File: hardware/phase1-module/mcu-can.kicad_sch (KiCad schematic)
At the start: 29 parts, among them J2 SWD, J3 UART, U10 STM32G431CBT6, U11 TCAN1042HGV, Y1 8MHz

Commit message: Apply China-sourcing engineering changes across all boards + mechanical frame
All datasheet-verified before application (details hardware/SOURCING.md sF):
- TMUX1101 -> TS5A3166DBVR (LCSC availability; ts5a3166.pdf: pin POSITIONS
  identical - 1=NO 2=COM 3=GND 4=IN 5=V+; VIH 2.4V ok from 3.3V GPIO)
- TLV7011 DBVR -> DCKR: tlv7022.pdf shows DBV/DCK share one pinout, so
  footprint-only (SOT-353_SC-70-5); SOT-23-5 stock in China is nearly gone
- crystal load caps 10p -> 18p, both phases (CL=12pF China crystals; the
  HANDOVER-blessed alternative to hunting CL=8pF parts)
- Phase-1 inductor -> MWSA1707S-100MT (JLCPCB-verified 16.5A Isat/10.5A
  Irms vs 12A/8A required); value strings now dual-source Sunlord/Coilcraft
- module slot power + P2 output -> XT60PW-M (2-pin), backplane slots ->
  XT60PW-F; bus shunt -> 2x BVS-M-R0005 parallel (the exact-net checker
  caught RS1/RS2 placed one pin-span apart merging VBUS_IN into VBUS)
- 470u bulk -> THT radial D10; output MLCCs 22u -> 10u/50V X7S; buzzer ->
  MLT-8530 (fp placeholder)
All four checker chains green: 137/173/30/80 components.

hardware/MECHANICAL.md (frozen): 30mm slot pitch, P2 130x90 4-layer,
backplane ~330x100 2-layer 2oz, manager 100x80; cost-first stackup (1oz
outer + solder-reinforced bus, 2oz only if the thermal soak demands it);
inductor footprint = SUPERSET pattern accepting Sunlord 1707 AND Coilcraft
XAL1510 so the A/B pair is a pure part swap.

HANDOVER: sub-0.5V mV-accurate output DEFERRED to a future dedicated
linear post-regulator module (user decision 2026-07-18); buck floors
documented (P2 0.7V @30V bus, P1 0.5V).

Co-Authored-By: Claude Fable 5 <noreply@anthropic.com>
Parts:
- C66, C67: value 10p -> 18p
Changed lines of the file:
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@@
     (in_bom yes) (on_board yes) (dnp no)
     (property "Reference" "C66" (at 213.35999999999999 132.07999999999998 0) (effects (font (size 1.27 1.27)) (justify left)))
-    (property "Value" "10p" (at 213.35999999999999 134.62 0) (effects (font (size 1.27 1.27)) (justify left)))
+    (property "Value" "18p" (at 213.35999999999999 134.62 0) (effects (font (size 1.27 1.27)) (justify left)))
     (property "Footprint" "Capacitor_SMD:C_0603_1608Metric" (at 210.82 137.16 0) (effects (font (size 1.27 1.27)) hide))
     (property "Datasheet" "~" (at 210.82 137.16 0) (effects (font (size 1.27 1.27)) hide))
@@
     (in_bom yes) (on_board yes) (dnp no)
     (property "Reference" "C67" (at 228.6 132.07999999999998 0) (effects (font (size 1.27 1.27)) (justify left)))
-    (property "Value" "10p" (at 228.6 134.62 0) (effects (font (size 1.27 1.27)) (justify left)))
+    (property "Value" "18p" (at 228.6 134.62 0) (effects (font (size 1.27 1.27)) (justify left)))
     (property "Footprint" "Capacitor_SMD:C_0603_1608Metric" (at 226.06 137.16 0) (effects (font (size 1.27 1.27)) hide))
     (property "Datasheet" "~" (at 226.06 137.16 0) (effects (font (size 1.27 1.27)) hide))

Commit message: Add LCSC part numbers to all four boards' schematics and generate BOMs
common/bom.py writes hidden LCSC/MPN/Manufacturer properties into the
placed symbols (additive only, both one-line and KiCad multi-line
property styles) and emits <board>/bom/<board>-bom.csv plus a
JLCPCB-format CSV. Part table in common/lcsc_parts.py, transcribed
from SOURCING.md with explicit references per board; CHECK notes flag
footprint/variant mismatches. --check fails on stale output.

Co-Authored-By: Claude Opus 5.5 (1M context) <noreply@anthropic.com>
Claude-Session: https://claude.ai/code/session_01MKtKgebN9BpUrgqHq9t7pT
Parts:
- U10: LCSC (none) -> C529355; MPN (none) -> STM32G431CBT6; Manufacturer (none) -> ST
- U11: LCSC (none) -> C485806; MPN (none) -> TCAN1042VDRQ1; Manufacturer (none) -> TI
- Y1: LCSC (none) -> C400090
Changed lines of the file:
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@@
     (property "Footprint" "Package_QFP:LQFP-48_7x7mm_P0.5mm" (at 88.9 116.84 0) (effects (font (size 1.27 1.27)) hide))
     (property "Datasheet" "~" (at 88.9 116.84 0) (effects (font (size 1.27 1.27)) hide))
+    (property "LCSC" "C529355" (at 88.9 116.84 0) (effects (font (size 1.27 1.27)) hide))
+    (property "MPN" "STM32G431CBT6" (at 88.9 116.84 0) (effects (font (size 1.27 1.27)) hide))
+    (property "Manufacturer" "ST" (at 88.9 116.84 0) (effects (font (size 1.27 1.27)) hide))
     (pin "1")
     (pin "10")
@@
     (property "Footprint" "Crystal:Crystal_SMD_3225-4Pin_3.2x2.5mm" (at 218.44 127.0 0) (effects (font (size 1.27 1.27)) hide))
     (property "Datasheet" "~" (at 218.44 127.0 0) (effects (font (size 1.27 1.27)) hide))
+    (property "LCSC" "C400090" (at 218.44 127.0 0) (effects (font (size 1.27 1.27)) hide))
     (pin "1")
     (pin "2")
@@
     (property "Footprint" "Package_SO:SOIC-8_3.9x4.9mm_P1.27mm" (at 174.5 165.1 0) (effects (font (size 1.27 1.27)) hide))
     (property "Datasheet" "~" (at 174.5 165.1 0) (effects (font (size 1.27 1.27)) hide))
-    (pin "1")
-    (pin "2")
+    (property "LCSC" "C485806" (at 174.5 165.1 0) (effects (font (size 1.27 1.27)) hide))
+    (property "MPN" "TCAN1042VDRQ1" (at 174.5 165.1 0) (effects (font (size 1.27 1.27)) hide))
+    (property "Manufacturer" "TI" (at 174.5 165.1 0) (effects (font (size 1.27 1.27)) hide))
+    (pin "1")
+    (pin "2")

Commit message: Phase-1 BOM: LCSC numbers for every assembled part
Fill the 109 missing Phase-1 placements from the JLCPCB catalogue
(checked 2026-09-27, Basic parts where one fits), so 127 of 136
placements carry an LCSC number. J1-J6 and F1 stay hand-solder;
C17 and R17 are DNP.

Out-of-stock swaps: Q1-Q4 CSD18563Q5A -> NTMFS5C670NLT1G (SO-8FL,
same pinout), P1 U5 INA228AIDGSR -> INA228AQDGSRQ1. Y1 moves to the
CL = 12 pF version of the same crystal (C400090 was the 10 pF one).

Co-Authored-By: Claude Opus 5.5 (1M context) <noreply@anthropic.com>
Claude-Session: https://claude.ai/code/session_013uVohQZFdivAh43gw4mZtf
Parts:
- C62, C68, C69, C70, C71, C72, C73, C74: LCSC (none) -> C14663; MPN (none) -> CC0603KRX7R9BB104; Manufacturer (none) -> YAGEO
- C64: LCSC (none) -> C19666; MPN (none) -> CL10A475KO8NNNC; Manufacturer (none) -> Samsung Electro-Mechanics
- C65: LCSC (none) -> C15849; MPN (none) -> CL10A105KB8NNNC; Manufacturer (none) -> Samsung Electro-Mechanics
- C66, C67: LCSC (none) -> C1647; MPN (none) -> CL10C180JB8NNNC; Manufacturer (none) -> Samsung Electro-Mechanics
- D7: LCSC (none) -> C2286; MPN (none) -> KT-0603R; Manufacturer (none) -> Hubei KENTO Elec
- R60: LCSC (none) -> C25811; MPN (none) -> 0603WAF2003T5E; Manufacturer (none) -> UNI-ROYAL
- R61, R64, R65, R67, R68: LCSC (none) -> C25804; MPN (none) -> 0603WAF1002T5E; Manufacturer (none) -> UNI-ROYAL
- R62, R63: LCSC (none) -> C23162; MPN (none) -> 0603WAF4701T5E; Manufacturer (none) -> UNI-ROYAL
- R66: LCSC (none) -> C21190; MPN (none) -> 0603WAF1001T5E; Manufacturer (none) -> UNI-ROYAL
- RT1, RT2: LCSC (none) -> C2892547; MPN (none) -> KNTC0603/10KF3950; Manufacturer (none) -> KUU
- Y1: LCSC C400090 -> C403948; MPN (none) -> TAXM8M4RFDCET2T; Manufacturer (none) -> Yajingxin

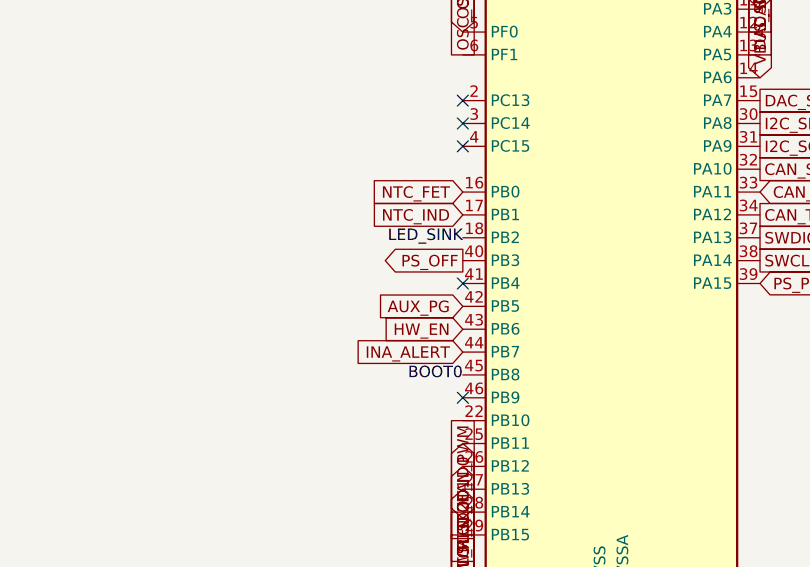
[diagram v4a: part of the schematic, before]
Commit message: Phase-1 board: route OVP_TRIP to MCU PB4 so the OVP trip can latch
The TLV7011 output only reached Q9 (disconnect), so an overvoltage
opened the output but left the LM5145 running and nothing latched.
OVP_TRIP now also goes to U10 pin 41 (PB4, a spare pin), where the
firmware 0.2 EXTI handler kills EN and latches OVP_HW.

Schematic: surgical edits (OVP_TRIP local labels -> global, PB4
no-connect -> OVP_TRIP label); gen_phase1.py / sheets_common.py
mirror it (ovp_to_mcu param, EXPECTED_NETS). check_netlist and
check_footprints pass.

Board: 21 signal nets in the U10-U7 region ripped and re-routed with
Freerouting 1.9 + finish_routes, fb_reroute rerun, three overlap stubs
trimmed. DRC: 0 unconnected, 0 errors, 10 silk warnings (was 11).
Fab zip regenerated; placement and BOM unchanged.

Co-Authored-By: Claude Opus 5.5 (1M context) <noreply@anthropic.com>
Claude-Session: https://claude.ai/code/session_01NmR2rbcK8CFj3PgzqsaRtW
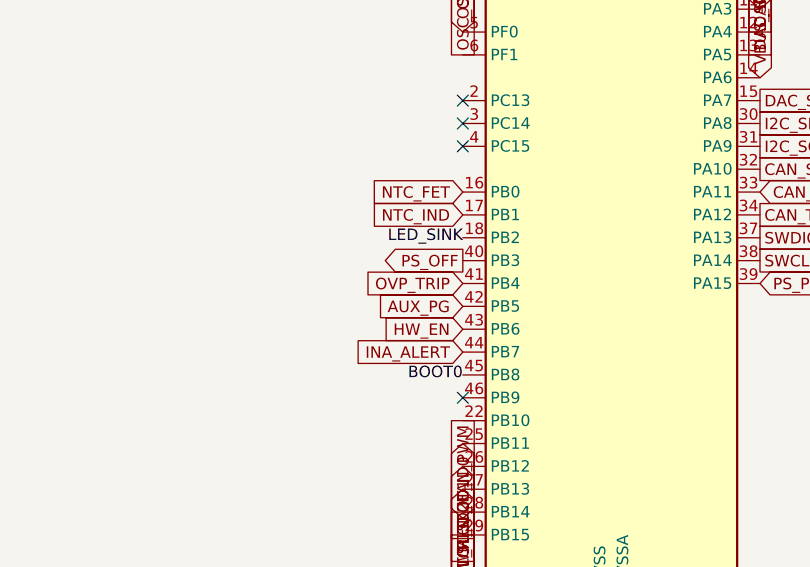
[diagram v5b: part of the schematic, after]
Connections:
- net OVP_TRIP: now reaches U10.41 (PB4)
- no-connect marks 5 -> 4
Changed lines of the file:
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@@
   (global_label "OUT_REQ" (shape output) (at 73.66 144.78 270) (fields_autoplaced) (effects (font (size 1.27 1.27))))
   (global_label "FAN_PWM" (shape output) (at 73.66 134.62 270) (fields_autoplaced) (effects (font (size 1.27 1.27))))
-  (no_connect (at 73.66 119.38))
+  (global_label "OVP_TRIP" (shape input) (at 73.66 119.38 180) (fields_autoplaced) (effects (font (size 1.27 1.27))))
   (no_connect (at 73.66 99.06))
   (no_connect (at 73.66 101.6))
